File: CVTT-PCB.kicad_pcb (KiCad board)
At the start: 4 copper layers, 66 x 88 mm, 67 parts, among them J1 SERVO1, J2 SERVO2, J3 LCD SCREEN, J4 LCD BUTTONS, J5 Conn_ARM_SWD_TagConnect_TC2030, J7 Barrel_Jack, P2 DC2, P5 DC1, P8 STEPPER, Q7 BSS138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

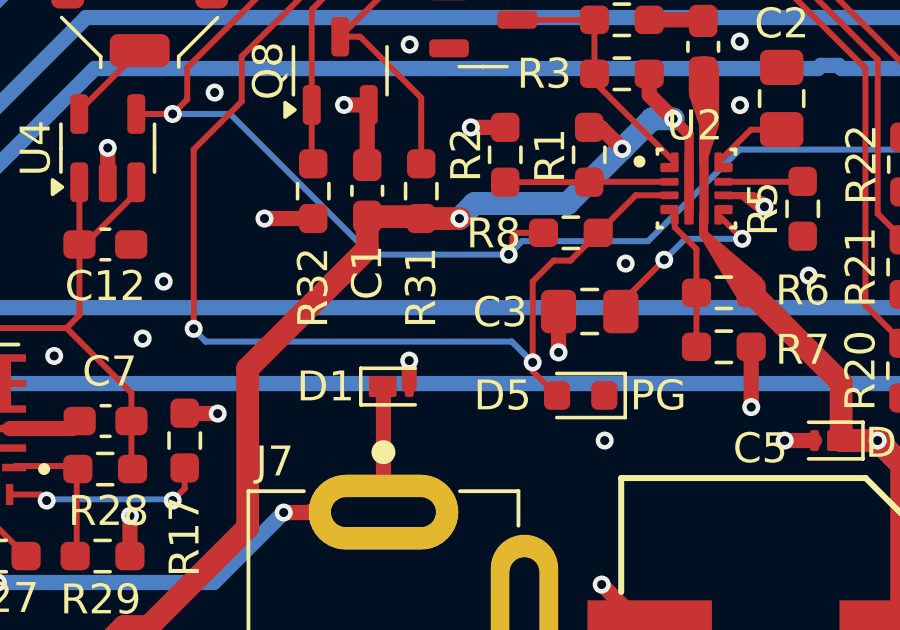
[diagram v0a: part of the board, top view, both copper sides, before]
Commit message: remove pg led
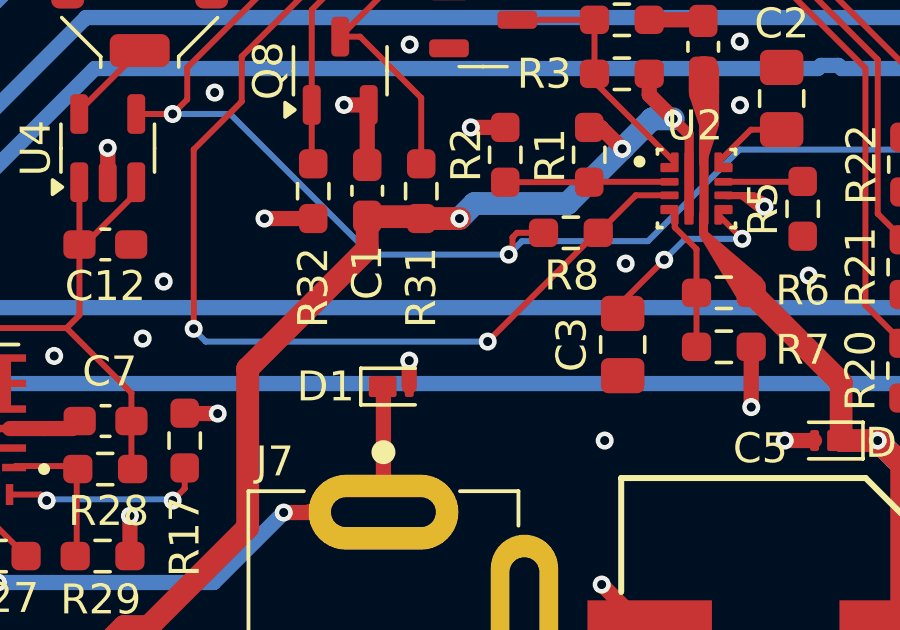
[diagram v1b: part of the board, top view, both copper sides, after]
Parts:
- removed D5: PG, LED_SMD:LED_0603_1608Metric
- R8: value 3.3k -> 47k
- moved C3 1.56 mm to (140.1, 124.8), turned to -90 degrees
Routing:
- net /PG: track 42.2 -> 38.6 mm
- net GND: track 49.1 -> 47.7 mm, vias 88 -> 87

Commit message: new pg
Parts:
- added D5: PG, LED_SMD:LED_0603_1608Metric, F.Cu at (135.7, 126.2)
- added REF**: MountingHole_2.7mm_M2.5_DIN965_Pad, MountingHole:MountingHole_2.7mm_M2.5_DIN965_Pad, F.Cu at (168.0, 136.5)
- added REF**: MountingHole_2.7mm_M2.5_DIN965_Pad, MountingHole:MountingHole_2.7mm_M2.5_DIN965_Pad, F.Cu at (110.0, 136.5)
- R8: value 47k -> 3.3k
- moved D3 0.99 mm to (117.9, 135.5)
- moved D4 0.99 mm to (117.9, 137.4)
- moved R15 0.99 mm to (124.1, 135.5)
- moved R16 0.99 mm to (124.1, 137.4)
- moved P8 0.58 mm to (109.3, 123.9)
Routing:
- net /PG: track 38.6 -> 40.6 mm
- net +3.3V: track 220.3 -> 221.3 mm
- net Net-(D3-K): track 39.8 -> 38.9 mm
- net Net-(A2-2B): track 52.6 -> 51.9 mm
- net GND: track 47.7 -> 48.0 mm, vias 87 -> 89

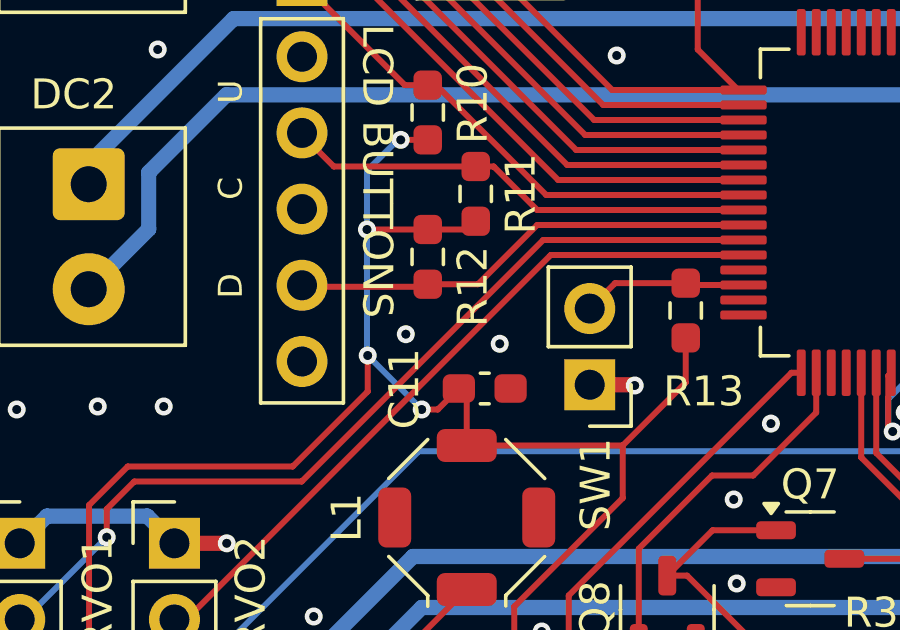
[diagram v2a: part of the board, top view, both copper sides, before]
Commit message: reconfigure ILM for motor req
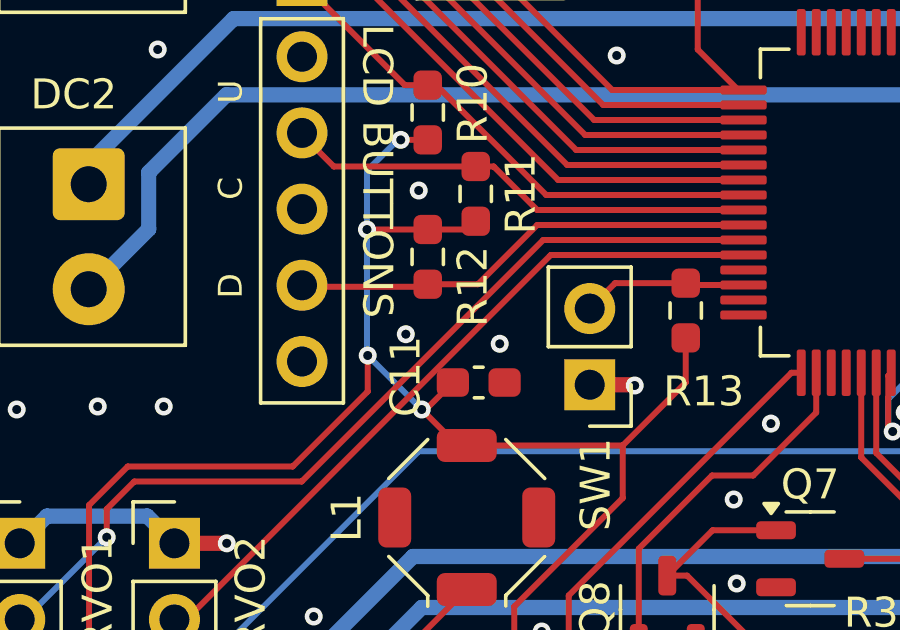
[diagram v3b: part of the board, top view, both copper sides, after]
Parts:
- R5: value 1k -> 510
- moved C11 0.28 mm to (124.4, 108.1)
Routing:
- net GND: vias 89 -> 90

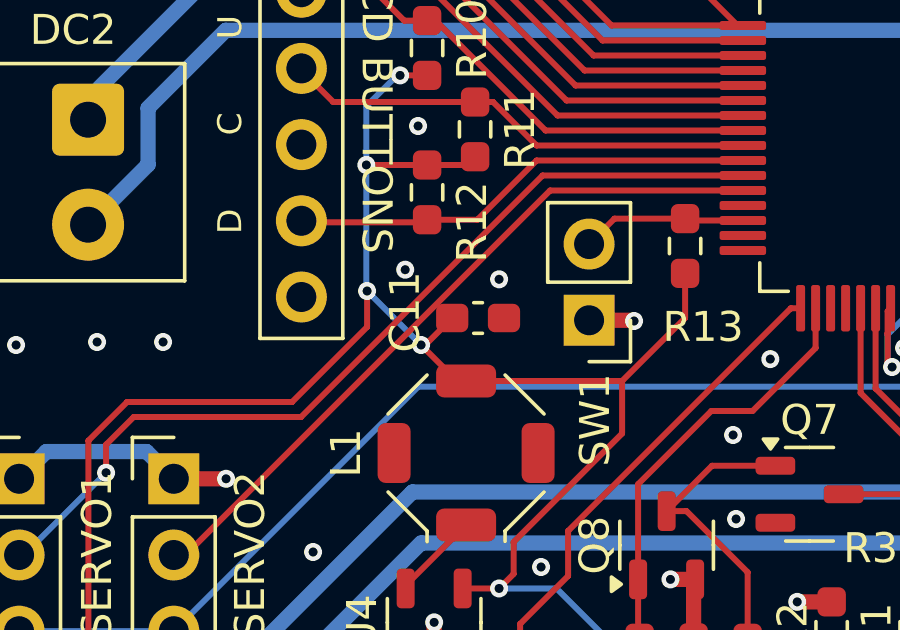
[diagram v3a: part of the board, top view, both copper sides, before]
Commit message: resolve DRC errors
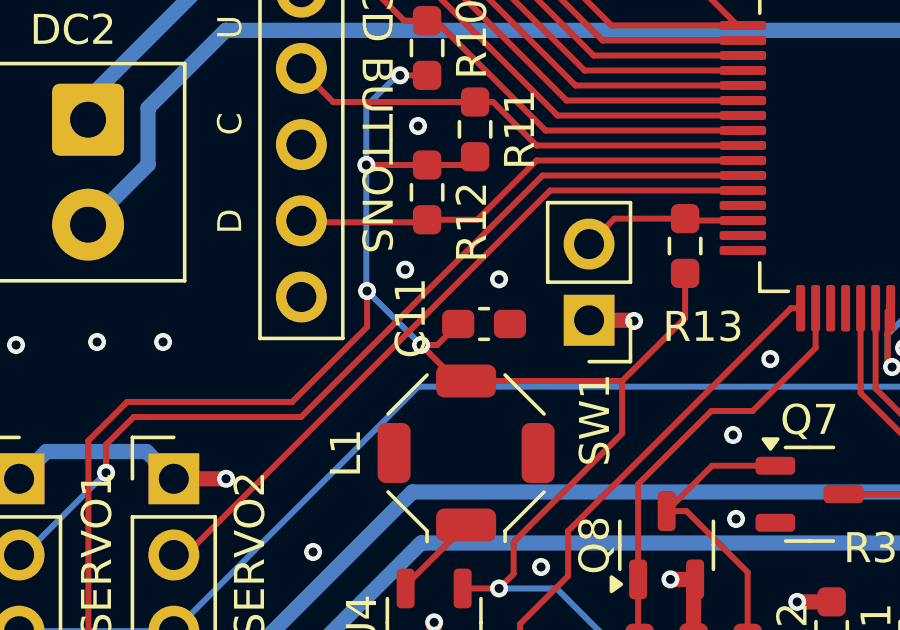
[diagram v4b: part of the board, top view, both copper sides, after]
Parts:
- moved C11 0.28 mm to (124.6, 108.3)

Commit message: final check before gerbers
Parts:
- U7: value RASPBERRY_PI_ZERO_2_W -> RASPBERRY PI ZERO 2 W

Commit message: pg placement
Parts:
- moved D5 16.0 mm to (133.0, 110.4)
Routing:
- net /PG: track 40.6 -> 38.0 mm
- net GND: track 48.0 -> 49.3 mm, vias 90 -> 91
- net /EFUSE_EN: track 14.4 -> 15.5 mm

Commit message: edit sch
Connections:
- net /PMWA renamed /PWMA
- net /PMWB renamed /PWMB
- C1 pad 1: Net-(D3-K) -> +12V
- R1 pad 1: Net-(D3-K) -> +12V
- R3 pad 1: Net-(D3-K) -> +12V
- R31 pad 1: Net-(D3-K) -> +12V
- U2 pad 5: Net-(D3-K) -> +12V
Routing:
- net Net-(D3-K): track 38.9 -> 4.96 mm, vias 3 -> 0
- net +12V: track 25.4 -> 53.4 mm, vias 2 -> 5
